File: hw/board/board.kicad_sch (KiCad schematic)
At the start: 7 parts, among them U1 XC7A35T-FTG256, U5 STM32F302CBTx, U6 W25Q128JVSIQTR

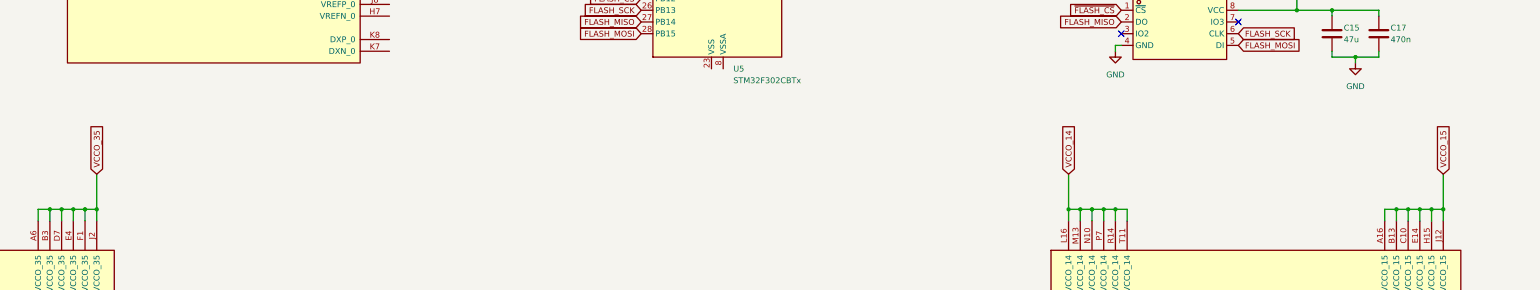
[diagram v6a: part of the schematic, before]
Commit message: Began refactoring BGA fanout
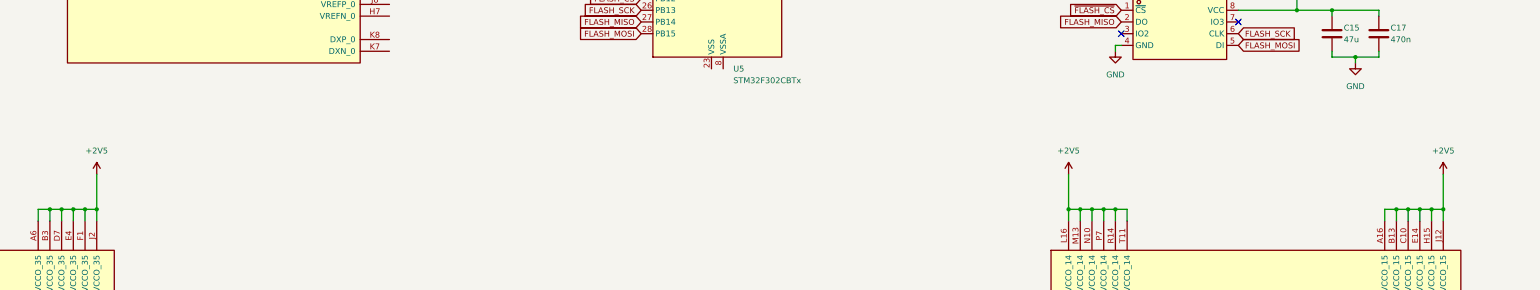
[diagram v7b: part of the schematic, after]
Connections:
- net VCCO_14 is gone; now on net +2V5: U1.L16 (VCCO_14), U1.M13 (VCCO_14), U1.N10 (VCCO_14), U1.P7 (VCCO_14), U1.R14 (VCCO_14), U1.T11 (VCCO_14)
- net VCCO_15 is gone; now on net +2V5: U1.A16 (VCCO_15), U1.B13 (VCCO_15), U1.C10 (VCCO_15), U1.E14 (VCCO_15), U1.H15 (VCCO_15), U1.J12 (VCCO_15)
- net VCCO_35 is gone; now on net +2V5: U1.A6 (VCCO_35), U1.B3 (VCCO_35), U1.D7 (VCCO_35), U1.E4 (VCCO_35), U1.F1 (VCCO_35), U1.J2 (VCCO_35)
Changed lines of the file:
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@@
 		)
 	)
-	(global_label "VCCO_14"
-		(shape input)
-		(at 344.17 137.16 90)
-		(fields_autoplaced yes)
-		(effects
-			(font
-				(size 1.27 1.27)
-			)
-			(justify left)
-		)
-		(property "Intersheetrefs" "${INTERSHEET_REFS}"
-			(at 344.17 125.8291 90)
-			(effects
-				(font
-					(size 1.27 1.27)
-				)
-				(justify left)
-				(hide yes)
-			)
-		)
-	)
 	(global_label "TDO"
 		(shape input)
@@
 		)
 	)
-	(global_label "VCCO_15"
-		(shape input)
-		(at 425.45 137.16 90)
-		(fields_autoplaced yes)
-		(effects
-			(font
-				(size 1.27 1.27)
-			)
-			(justify left)
-		)
-		(property "Intersheetrefs" "${INTERSHEET_REFS}"
-			(at 425.45 125.8291 90)
-			(effects
-				(font
-					(size 1.27 1.27)
-				)
-				(justify left)
-				(hide yes)
-			)
-		)
-	)
 	(global_label "S_{out}5_P"
 		(shape output)
@@
 		)
 	)
-	(global_label "VCCO_35"
-		(shape input)
-		(at 133.35 137.16 90)
-		(fields_autoplaced yes)
-		(effects
-			(font
-				(size 1.27 1.27)
-			)
-			(justify left)
-		)
-		(property "Intersheetrefs" "${INTERSHEET_REFS}"
-			(at 133.35 125.8291 90)
-			(effects
-				(font
-					(size 1.27 1.27)
-				)
-				(justify left)
-				(hide yes)
-			)
-		)
-	)
 	(global_label "CCLK"
 		(shape input)
@@
 	)
 	(symbol
+		(lib_id "power:+2V5")
+		(at 133.35 137.16 0)
+		(unit 1)
+		(exclude_from_sim no)
+		(in_bom yes)
+		(on_board yes)
+		(dnp no)
+		(fields_autoplaced yes)
+		(property "Reference" "#PWR041"
+			(at 133.35 140.97 0)
+			(effects
+				(font
+					(size 1.27 1.27)
+				)
+				(hide yes)
+			)
+		)
+		(property "Value" "+2V5"
+			(at 133.35 132.08 0)
+			(effects
+				(font
+					(size 1.27 1.27)
+				)
+			)
+		)
+		(property "Footprint" ""
+			(at 133.35 137.16 0)
+			(effects
+				(font
+					(size 1.27 1.27)
+				)
+				(hide yes)
+			)
+		)
+		(property "Datasheet" ""
+			(at 133.35 137.16 0)
+			(effects
+				(font
+					(size 1.27 1.27)
+				)
+				(hide yes)
+			)
+		)
+		(property "Description" "Power symbol creates a global label with name \"+2V5\""
+			(at 133.35 137.16 0)
+			(effects
+				(font
+					(size 1.27 1.27)
+				)
+				(hide yes)
+			)
+		)
+		(pin "1"
+		)
+		(instances
+			(project "board"
+				(path "/0e384709-6bce-4dbf-a0e0-550e970390f4"
+					(reference "#PWR041")
+					(unit 1)
+				)
+			)
+		)
+	)
+	(symbol
 		(lib_id "Device:C")
 		(at 401.32 106.68 0)
@@
 	)
 	(symbol
+		(lib_id "power:+2V5")
+		(at 344.17 137.16 0)
+		(unit 1)
+		(exclude_from_sim no)
+		(in_bom yes)
+		(on_board yes)
+		(dnp no)
+		(fields_autoplaced yes)
+		(property "Reference" "#PWR042"
+			(at 344.17 140.97 0)
+			(effects
+				(font
+					(size 1.27 1.27)
+				)
+				(hide yes)
+			)
+		)
+		(property "Value" "+2V5"
+			(at 344.17 132.08 0)
+			(effects
+				(font
+					(size 1.27 1.27)
+				)
+			)
+		)
+		(property "Footprint" ""
+			(at 344.17 137.16 0)
+			(effects
+				(font
+					(size 1.27 1.27)
+				)
+				(hide yes)
+			)
+		)
+		(property "Datasheet" ""
+			(at 344.17 137.16 0)
+			(effects
+				(font
+					(size 1.27 1.27)
+				)
+				(hide yes)
+			)
+		)
+		(property "Description" "Power symbol creates a global label with name \"+2V5\""
+			(at 344.17 137.16 0)
+			(effects
+				(font
+					(size 1.27 1.27)
+				)
+				(hide yes)
+			)
+		)
+		(pin "1"
+		)
+		(instances
+			(project "board"
+				(path "/0e384709-6bce-4dbf-a0e0-550e970390f4"
+					(reference "#PWR042")
+					(unit 1)
+				)
+			)
+		)
+	)
+	(symbol
 		(lib_id "Device:C")
 		(at 411.48 106.68 0)
@@
 					(unit 1)
 				)
+			)
+		)
+	)
+	(symbol
+		(lib_id "power:+2V5")
+		(at 425.45 137.16 0)
+		(unit 1)
+		(exclude_from_sim no)
+		(in_bom yes)
+		(on_board yes)
+		(dnp no)
+		(fields_autoplaced yes)
+		(property "Reference" "#PWR043"
+			(at 425.45 140.97 0)
+			(effects
+				(font
+					(size 1.27 1.27)
+				)
+				(hide yes)
+			)
+		)
+		(property "Value" "+2V5"
+			(at 425.45 132.08 0)
+			(effects
+				(font
+					(size 1.27 1.27)
+				)
+			)
+		)
+		(property "Footprint" ""
+			(at 425.45 137.16 0)
+			(effects
+				(font
+					(size 1.27 1.27)
+				)
+				(hide yes)
+			)
+		)
+		(property "Datasheet" ""
+			(at 425.45 137.16 0)
+			(effects
+				(font
+					(size 1.27 1.27)
+				)
+				(hide yes)
+			)
+		)
+		(property "Description" "Power symbol creates a global label with name \"+2V5\""
+			(at 425.45 137.16 0)
+			(effects
+				(font
+					(size 1.27 1.27)
+				)
+				(hide yes)
+			)
+		)
+		(pin "1"
+		)
+		(instances
+			(project "board"
+				(path "/0e384709-6bce-4dbf-a0e0-550e970390f4"
+					(reference "#PWR043")
+					(unit 1)
+				)
